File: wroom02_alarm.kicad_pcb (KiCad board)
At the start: 2 copper layers, 50 x 50 mm, 93 parts, among them J1 Serial, J10 pin, J11 pin, J12 pin, J13 pin, J14 pin, J15 pin, J2 pin, J3 microUSB, J4 pin, J5 pin, J6 pin, J7 pin, J8 pin, J9 pin, Q1 Q_NMOS_GDS, SW1 Write, SW2 RESET, U1 wroom02, U3 7803

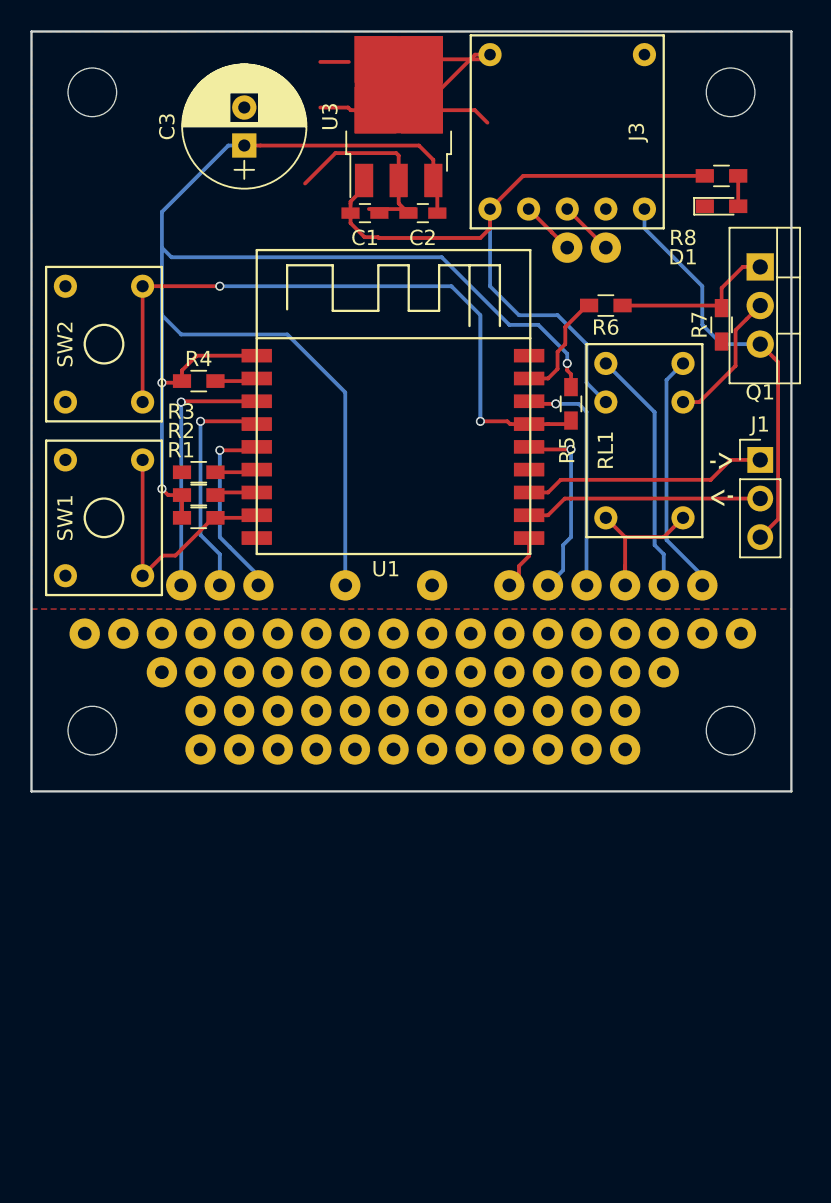
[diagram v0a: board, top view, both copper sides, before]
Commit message: 基板サイズを変更
Fusionにドリルが多すぎるって怒られた．
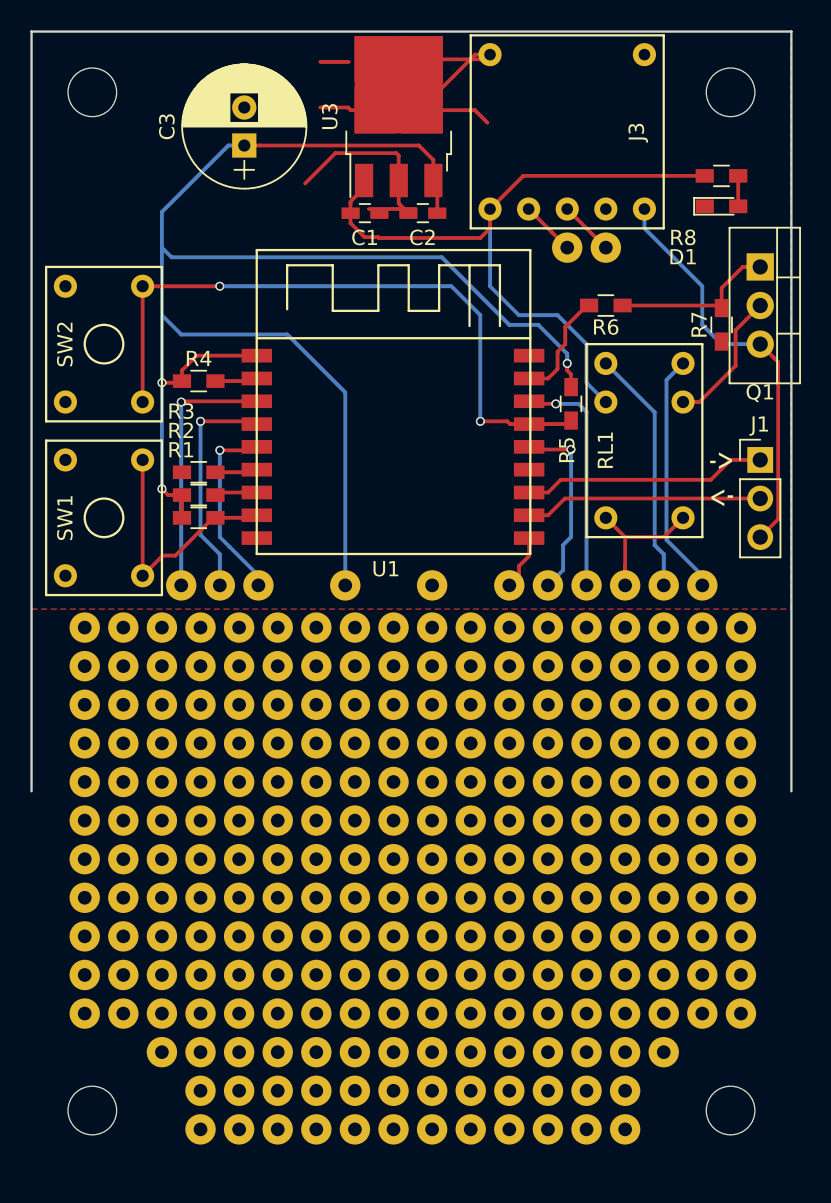
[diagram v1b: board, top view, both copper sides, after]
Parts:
- added REF**: , pad:universal, F.Cu at (73.7, 134.2)
- added REF**: , pad:universal, F.Cu at (96.5, 134.2)
- added REF**: , pad:universal, F.Cu at (91.4, 146.9)
- added REF**: , pad:universal, F.Cu at (88.9, 146.9)
- added REF**: , pad:universal, F.Cu at (94.0, 149.5)
- added REF**: , pad:universal, F.Cu at (91.4, 152.0)
- added REF**: , pad:universal, F.Cu at (94.0, 152.0)
- added REF**: , pad:universal, F.Cu at (86.4, 152.0)
- added REF**: , pad:universal, F.Cu at (88.9, 152.0)
- added REF**: , pad:universal, F.Cu at (71.1, 146.9)
- added REF**: , pad:universal, F.Cu at (73.7, 146.9)
- added REF**: , pad:universal, F.Cu at (73.7, 149.5)
- added REF**: , pad:universal, F.Cu at (99.1, 134.2)
- added REF**: , pad:universal, F.Cu at (71.1, 149.5)
- added REF**: , pad:universal, F.Cu at (68.6, 146.9)
- added REF**: , pad:universal, F.Cu at (63.5, 149.5)
- added REF**: , pad:universal, F.Cu at (68.6, 149.5)
- added REF**: , pad:universal, F.Cu at (63.5, 146.9)
- added REF**: , pad:universal, F.Cu at (68.6, 152.0)
- added REF**: , pad:universal, F.Cu at (66.0, 149.5)
- added REF**: , pad:universal, F.Cu at (66.0, 146.9)
- added REF**: , pad:universal, F.Cu at (73.7, 152.0)
- added REF**: , pad:universal, F.Cu at (71.1, 152.0)
- added REF**: , pad:universal, F.Cu at (101.6, 134.2)
- added REF**: , pad:universal, F.Cu at (63.5, 152.0)
- added REF**: , pad:universal, F.Cu at (66.0, 152.0)
- added REF**: , pad:universal, F.Cu at (78.7, 146.9)
- added REF**: , pad:universal, F.Cu at (78.7, 149.5)
- added REF**: , pad:universal, F.Cu at (81.3, 149.5)
- added REF**: , pad:universal, F.Cu at (81.3, 146.9)
- added REF**: , pad:universal, F.Cu at (83.8, 146.9)
- added REF**: , pad:universal, F.Cu at (83.8, 149.5)
- added REF**: , pad:universal, F.Cu at (81.3, 152.0)
- added REF**: , pad:universal, F.Cu at (83.8, 152.0)
- added REF**: , pad:universal, F.Cu at (106.7, 134.2)
- added REF**: , pad:universal, F.Cu at (76.2, 146.9)
- added REF**: , pad:universal, F.Cu at (76.2, 149.5)
- added REF**: , pad:universal, F.Cu at (78.7, 152.0)
- added REF**: , pad:universal, F.Cu at (76.2, 152.0)
- added REF**: , pad:universal, F.Cu at (101.6, 146.9)
- added REF**: , pad:universal, F.Cu at (104.1, 149.5)
- added REF**: , pad:universal, F.Cu at (101.6, 149.5)
- added REF**: , pad:universal, F.Cu at (104.1, 146.9)
- added REF**: , pad:universal, F.Cu at (106.7, 149.5)
- added REF**: , pad:universal, F.Cu at (106.7, 146.9)
- added REF**: , pad:universal, F.Cu at (104.1, 134.2)
- added REF**: , pad:universal, F.Cu at (101.6, 152.0)
- added REF**: , pad:universal, F.Cu at (96.5, 152.0)
- added REF**: , pad:universal, F.Cu at (99.1, 152.0)
- added REF**: , pad:universal, F.Cu at (104.1, 152.0)
- added REF**: , pad:universal, F.Cu at (106.7, 152.0)
- added REF**: , pad:universal, F.Cu at (73.7, 154.5)
- added REF**: , pad:universal, F.Cu at (71.1, 154.5)
- added REF**: , pad:universal, F.Cu at (66.0, 154.5)
- added REF**: , pad:universal, F.Cu at (63.5, 154.5)
- added REF**: , pad:universal, F.Cu at (68.6, 154.5)
- added REF**: , pad:universal, F.Cu at (68.6, 134.2)
- added REF**: , pad:universal, F.Cu at (83.8, 154.5)
- added REF**: , pad:universal, F.Cu at (81.3, 154.5)
- added REF**: , pad:universal, F.Cu at (76.2, 154.5)
- added REF**: , pad:universal, F.Cu at (78.7, 154.5)
- added REF**: , pad:universal, F.Cu at (99.1, 154.5)
- added REF**: , pad:universal, F.Cu at (96.5, 154.5)
- added REF**: , pad:universal, F.Cu at (94.0, 154.5)
- added REF**: , pad:universal, F.Cu at (91.4, 154.5)
- added REF**: , pad:universal, F.Cu at (106.7, 154.5)
- added REF**: , pad:universal, F.Cu at (104.1, 154.5)
- added REF**: , pad:universal, F.Cu at (63.5, 134.2)
- added REF**: , pad:universal, F.Cu at (101.6, 154.5)
- added REF**: , pad:universal, F.Cu at (88.9, 154.5)
- added REF**: , pad:universal, F.Cu at (86.4, 154.5)
- added REF**: , pad:universal, F.Cu at (73.7, 157.1)
- added REF**: , pad:universal, F.Cu at (71.1, 157.1)
- added REF**: , pad:universal, F.Cu at (66.0, 157.1)
- added REF**: , pad:universal, F.Cu at (63.5, 157.1)
- added REF**: , pad:universal, F.Cu at (68.6, 157.1)
- added REF**: , pad:universal, F.Cu at (83.8, 157.1)
- added REF**: , pad:universal, F.Cu at (81.3, 157.1)
- added REF**: , pad:universal, F.Cu at (71.1, 134.2)
- added REF**: , pad:universal, F.Cu at (76.2, 157.1)
- added REF**: , pad:universal, F.Cu at (78.7, 157.1)
- added REF**: , pad:universal, F.Cu at (99.1, 157.1)
- added REF**: , pad:universal, F.Cu at (96.5, 157.1)
- added REF**: , pad:universal, F.Cu at (94.0, 157.1)
- added REF**: , pad:universal, F.Cu at (91.4, 157.1)
- added REF**: , pad:universal, F.Cu at (106.7, 157.1)
- added REF**: , pad:universal, F.Cu at (104.1, 157.1)
- added REF**: , pad:universal, F.Cu at (101.6, 157.1)
- added REF**: , pad:universal, F.Cu at (88.9, 157.1)
- added REF**: , pad:universal, F.Cu at (66.0, 134.2)
- added REF**: , pad:universal, F.Cu at (86.4, 157.1)
- added REF**: , pad:universal, F.Cu at (94.0, 136.8)
- added REF**: , pad:universal, F.Cu at (76.2, 134.2)
- added REF**: , pad:universal, F.Cu at (88.9, 136.8)
- added REF**: , pad:universal, F.Cu at (88.9, 139.3)
- added REF**: , pad:universal, F.Cu at (91.4, 136.8)
- added REF**: , pad:universal, F.Cu at (94.0, 139.3)
- added REF**: , pad:universal, F.Cu at (91.4, 139.3)
- added REF**: , pad:universal, F.Cu at (86.4, 136.8)
- added REF**: , pad:universal, F.Cu at (86.4, 141.8)
- added REF**: , pad:universal, F.Cu at (86.4, 139.3)
- added REF**: , pad:universal, F.Cu at (91.4, 141.8)
- added REF**: , pad:universal, F.Cu at (88.9, 141.8)
- added REF**: , pad:universal, F.Cu at (86.4, 134.2)
- added REF**: , pad:universal, F.Cu at (96.5, 136.8)
- added REF**: , pad:universal, F.Cu at (99.1, 141.8)
- added REF**: , pad:universal, F.Cu at (96.5, 144.4)
- added REF**: , pad:universal, F.Cu at (99.1, 139.3)
- added REF**: , pad:universal, F.Cu at (96.5, 139.3)
- added REF**: , pad:universal, F.Cu at (99.1, 136.8)
- added REF**: , pad:universal, F.Cu at (96.5, 141.8)
- added REF**: , pad:universal, F.Cu at (99.1, 144.4)
- added REF**: , pad:universal, F.Cu at (104.1, 144.4)
- added REF**: , pad:universal, F.Cu at (106.7, 144.4)
- added REF**: , pad:universal, F.Cu at (83.8, 134.2)
- added REF**: , pad:universal, F.Cu at (106.7, 141.8)
- added REF**: , pad:universal, F.Cu at (101.6, 136.8)
- added REF**: , pad:universal, F.Cu at (101.6, 139.3)
- added REF**: , pad:universal, F.Cu at (106.7, 139.3)
- added REF**: , pad:universal, F.Cu at (106.7, 136.8)
- added REF**: , pad:universal, F.Cu at (104.1, 139.3)
- added REF**: , pad:universal, F.Cu at (104.1, 136.8)
- added REF**: , pad:universal, F.Cu at (88.9, 144.4)
- added REF**: , pad:universal, F.Cu at (86.4, 144.4)
- added REF**: , pad:universal, F.Cu at (91.4, 144.4)
- added REF**: , pad:universal, F.Cu at (78.7, 134.2)
- added REF**: , pad:universal, F.Cu at (94.0, 144.4)
- added REF**: , pad:universal, F.Cu at (73.7, 141.8)
- added REF**: , pad:universal, F.Cu at (73.7, 144.4)
- added REF**: , pad:universal, F.Cu at (78.7, 141.8)
- added REF**: , pad:universal, F.Cu at (76.2, 141.8)
- added REF**: , pad:universal, F.Cu at (78.7, 144.4)
- added REF**: , pad:universal, F.Cu at (76.2, 144.4)
- added REF**: , pad:universal, F.Cu at (71.1, 144.4)
- added REF**: , pad:universal, F.Cu at (63.5, 141.8)
- added REF**: , pad:universal, F.Cu at (68.6, 144.4)
- added REF**: , pad:universal, F.Cu at (81.3, 134.2)
- added REF**: , pad:universal, F.Cu at (66.0, 144.4)
- added REF**: , pad:universal, F.Cu at (63.5, 144.4)
- added REF**: , pad:universal, F.Cu at (66.0, 141.8)
- added REF**: , pad:universal, F.Cu at (71.1, 136.8)
- added REF**: , pad:universal, F.Cu at (73.7, 139.3)
- added REF**: , pad:universal, F.Cu at (73.7, 136.8)
- added REF**: , pad:universal, F.Cu at (71.1, 139.3)
- added REF**: , pad:universal, F.Cu at (68.6, 136.8)
- added REF**: , pad:universal, F.Cu at (68.6, 139.3)
- added REF**: , pad:universal, F.Cu at (68.6, 141.8)
- added REF**: , pad:universal, F.Cu at (94.0, 134.2)
- added REF**: , pad:universal, F.Cu at (71.1, 141.8)
- added REF**: , pad:universal, F.Cu at (63.5, 139.3)
- added REF**: , pad:universal, F.Cu at (63.5, 136.8)
- added REF**: , pad:universal, F.Cu at (66.0, 136.8)
- added REF**: , pad:universal, F.Cu at (66.0, 139.3)
- added REF**: , pad:universal, F.Cu at (81.3, 139.3)
- added REF**: , pad:universal, F.Cu at (83.8, 136.8)
- added REF**: , pad:universal, F.Cu at (83.8, 139.3)
- added REF**: , pad:universal, F.Cu at (81.3, 136.8)
- added REF**: , pad:universal, F.Cu at (83.8, 141.8)
- added REF**: , pad:universal, F.Cu at (91.4, 134.2)
- added REF**: , pad:universal, F.Cu at (81.3, 141.8)
- added REF**: , pad:universal, F.Cu at (81.3, 144.4)
- added REF**: , pad:universal, F.Cu at (83.8, 144.4)
- added REF**: , pad:universal, F.Cu at (78.7, 136.8)
- added REF**: , pad:universal, F.Cu at (78.7, 139.3)
- added REF**: , pad:universal, F.Cu at (76.2, 139.3)
- added REF**: , pad:universal, F.Cu at (76.2, 136.8)
- added REF**: , pad:universal, F.Cu at (94.0, 141.8)
- added REF**: , pad:universal, F.Cu at (101.6, 141.8)
- added REF**: , pad:universal, F.Cu at (101.6, 144.4)
- added REF**: , pad:universal, F.Cu at (88.9, 134.2)
- added REF**: , pad:universal, F.Cu at (104.1, 141.8)
- added REF**: , pad:universal, F.Cu at (94.0, 146.9)
- added REF**: , pad:universal, F.Cu at (96.5, 146.9)
- added REF**: , pad:universal, F.Cu at (99.1, 149.5)
- added REF**: , pad:universal, F.Cu at (96.5, 149.5)
- added REF**: , pad:universal, F.Cu at (99.1, 146.9)
- added REF**: , pad:universal, F.Cu at (86.4, 146.9)
- added REF**: , pad:universal, F.Cu at (91.4, 149.5)
- added REF**: , pad:universal, F.Cu at (88.9, 149.5)
- added REF**: , pad:universal, F.Cu at (86.4, 149.5)
- moved REF** 25.0 mm to (106.7, 159.6)
- moved REF** 25.0 mm to (101.6, 162.2)
- moved REF** 25.0 mm to (104.1, 159.6)
- moved REF** 25.0 mm to (101.6, 159.6)
- moved REF** 25.0 mm to (99.1, 167.2)
- moved REF** 25.0 mm to (99.1, 164.7)
- moved REF** 25.0 mm to (99.1, 162.2)
- moved REF** 25.0 mm to (96.5, 162.2)
- moved REF** 25.0 mm to (96.5, 164.7)
- moved REF** 25.0 mm to (96.5, 167.2)
- moved REF** 25.0 mm to (99.1, 159.6)
- moved REF** 25.0 mm to (96.5, 159.6)
- moved REF** 25.0 mm to (94.0, 167.2)
- moved REF** 25.0 mm to (94.0, 164.7)
- moved REF** 25.0 mm to (94.0, 162.2)
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
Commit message: GBRを作成
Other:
- board size 50 x 50 mm -> 50 x 75 mm
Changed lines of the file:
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@@
     (links 64)
     (no_connects 0)
-    (area 54.442857 93.825 132.85 157.700001)
+    (area 54.442857 93.825 128.85 182.849575)
     (thickness 1.6)
-    (drawings 22)
+    (drawings 20)
     (tracks 191)
     (zones 0)
@@
     (41 Cmts.User user)
     (42 Eco1.User user)
-    (43 Eco2.User user)
+    (43 Eco2.User user hide)
     (44 Edge.Cuts user)
     (45 Margin user)
@@
     (pad 1 thru_hole circle (at 0 0) (size 2 2) (drill 0.9) (layers *.Cu *.Mask))
   )
-  (gr_line (start 60 170) (end 60 145) (layer Eco2.User) (width 0.2))
-  (gr_line (start 110 170) (end 60 170) (layer Eco2.User) (width 0.2))
-  (gr_line (start 110 145) (end 110 170) (layer Eco2.User) (width 0.2))
+  (gr_line (start 110 170) (end 110 95) (angle 90) (layer Edge.Cuts) (width 0.15))
+  (gr_line (start 60 170) (end 110 170) (angle 90) (layer Edge.Cuts) (width 0.15))
+  (gr_line (start 60 95) (end 60 170) (angle 90) (layer Edge.Cuts) (width 0.15))
+  (gr_line (start 110 95) (end 60 95) (angle 90) (layer Edge.Cuts) (width 0.15))
   (dimension 75 (width 0.3) (layer Eco2.User)
     (gr_text "75.000 mm" (at 122.35 132.5 90) (layer Eco2.User)
@@
     (effects (font (size 1.5 1.5) (thickness 0.3)) (justify mirror))
   )
-  (gr_line (start 60 95) (end 110 95) (angle 90) (layer Edge.Cuts) (width 0.15))
-  (gr_line (start 60 145) (end 60 95) (angle 90) (layer Edge.Cuts) (width 0.15))
-  (gr_line (start 110 95) (end 110 145) (angle 90) (layer Edge.Cuts) (width 0.15))
   (dimension 50 (width 0.3) (layer Eco2.User)
     (gr_text "50.000 mm" (at 84.82531 181.499574) (layer Eco2.User)
